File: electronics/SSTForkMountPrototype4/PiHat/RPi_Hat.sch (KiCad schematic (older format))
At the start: 14 parts, among them CON1 BARREL_JACK, J1 RJ12, K1 G5LE-1A, K2 G5LE-1A, SW1 SW_SPST, U1 VOD223T, U2 pololu_D24V22F5, U3 Teensy_3.1, U4 SparkFun_BigEasyDriver, U5 SparkFun_BigEasyDriver

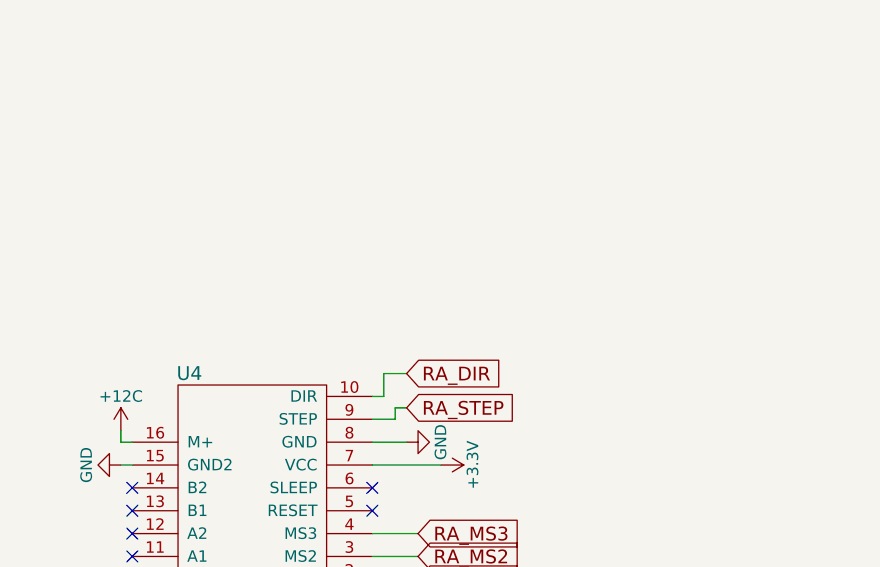
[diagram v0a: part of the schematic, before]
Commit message: Note on stepper motor test point voltage added.
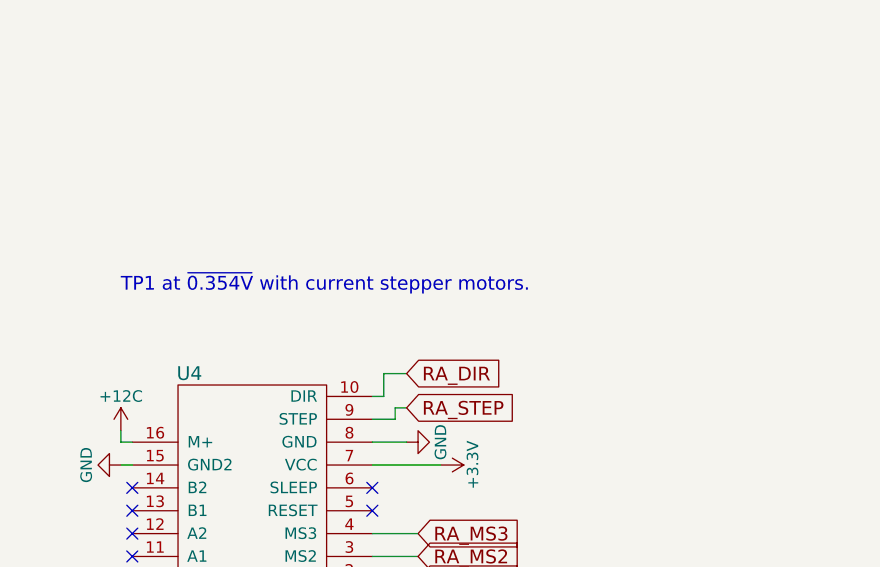
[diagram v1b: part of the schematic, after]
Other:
- note added: "TP1 at ~0.354V with current stepper motors."
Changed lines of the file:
@@
 Wire Wire Line
 	3900 2800 4000 2800
+Text Notes 1200 4850 0    60   ~ 0
+TP1 at ~0.354V with current stepper motors.
 $EndSCHEMATC

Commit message: Updated notes
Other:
- note added: "TP1 at ~0.354V with current stepper motors.\nAlso cut APWR jumper"
- note removed: "TP1 at ~0.354V with current stepper motors."
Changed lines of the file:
@@
 	3900 2800 4000 2800
 Text Notes 1200 4850 0    60   ~ 0
-TP1 at ~0.354V with current stepper motors.
+TP1 at ~0.354V with current stepper motors.\nAlso cut APWR jumper
 $EndSCHEMATC

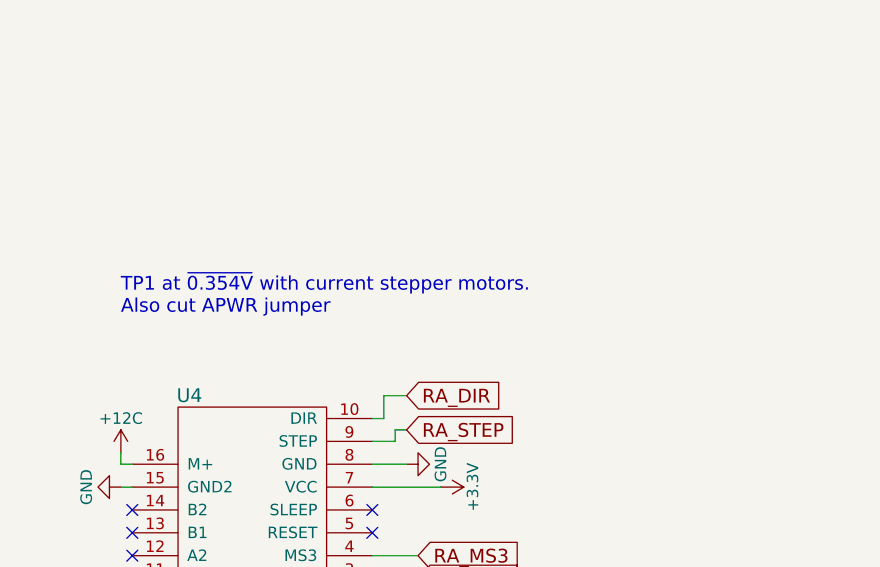
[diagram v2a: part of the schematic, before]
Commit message: Enable power switch detection to shutdown.
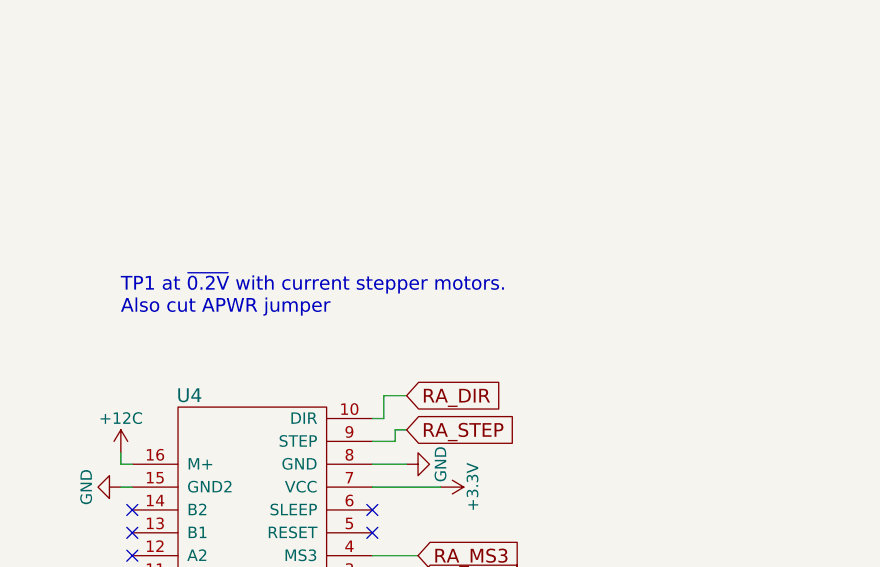
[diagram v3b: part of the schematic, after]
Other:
- note added: "TP1 at ~0.2V with current stepper motors.\nAlso cut APWR jumper"
- note removed: "TP1 at ~0.354V with current stepper motors.\nAlso cut APWR jumper"
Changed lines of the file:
@@
 	3900 2800 4000 2800
 Text Notes 1200 4850 0    60   ~ 0
-TP1 at ~0.354V with current stepper motors.\nAlso cut APWR jumper
+TP1 at ~0.2V with current stepper motors.\nAlso cut APWR jumper
 $EndSCHEMATC
